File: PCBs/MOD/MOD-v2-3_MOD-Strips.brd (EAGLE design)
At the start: 50.8 x 25.4 mm, 11 parts

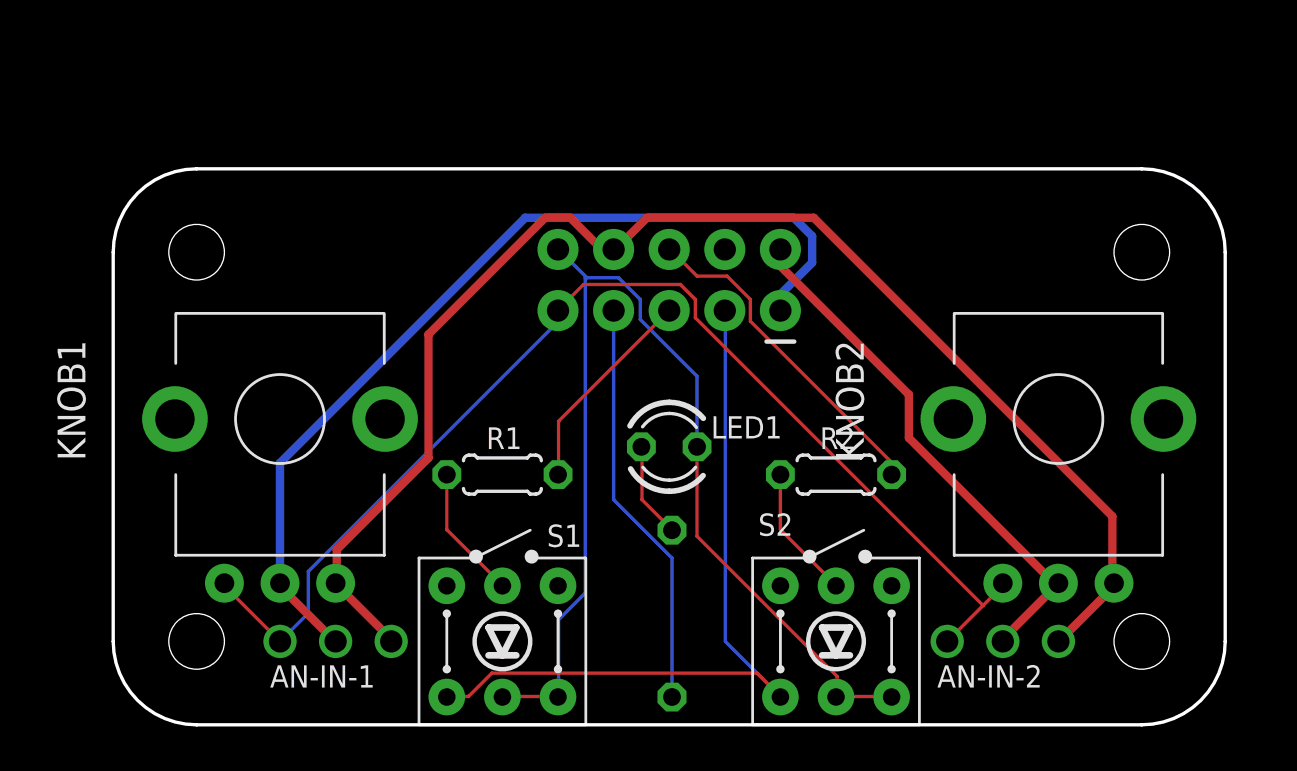
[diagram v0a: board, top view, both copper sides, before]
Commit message: new MOD teensy board
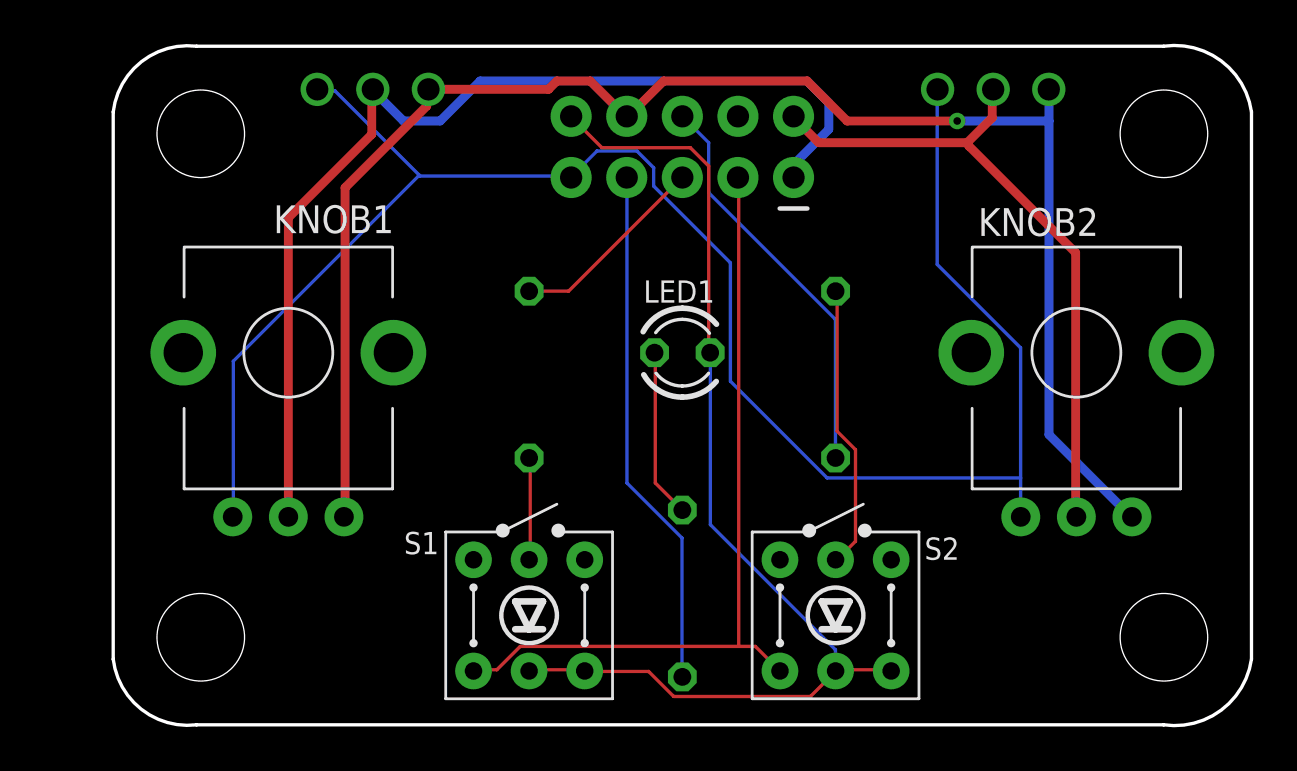
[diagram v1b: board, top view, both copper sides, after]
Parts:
- removed J1: (no value), SparkFun-Connectors:2X5-SHROUDED_LOCK
- added STRIP-MOD: (no value), SparkFun-Connectors:2X5-SHROUDED_LOCK
- R1, R2: device CMU-ArtFab:0204/5 -> CMU-ArtFab:0204/7
- moved AN-IN-1 25.3 mm to (9.32, 29.0), flipped to the bottom, turned to 180 degrees
- moved AN-IN-2 25.2 mm to (37.7, 29.0), flipped to the bottom, turned to 180 degrees
- moved R1 4.73 mm to (19.0, 16.0), flipped to the bottom, turned to 90 degrees
- moved R2 4.57 mm to (33.0, 16.0), flipped to the bottom, turned to 270 degrees
- moved LED1 4.34 mm to (26.0, 17.0)
- moved KNOB2 3.14 mm to (44.0, 17.0)
- moved KNOB1 3.05 mm to (8.00, 17.0)
- moved S1 1.70 mm to (19.0, 5.00)
- moved S2 1.19 mm to (33.0, 5.00)
- moved R4 1.03 mm to (26.0, 6.00)
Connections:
- net +3V3: now also STRIP-MOD.9; no longer J1.9
- net AGND: now also STRIP-MOD.8; no longer J1.8
- net AN1: now also STRIP-MOD.1; no longer J1.1
- net AN2: now also STRIP-MOD.2; no longer J1.2
- net B1: now also STRIP-MOD.3; no longer J1.3
- net B2: now also STRIP-MOD.4; no longer J1.4
- net GND: now also STRIP-MOD.10; no longer J1.10
- net LED1: now also STRIP-MOD.7; no longer J1.7
- net PWM_1: now also STRIP-MOD.5; no longer J1.5
- net PWM_2: now also STRIP-MOD.6; no longer J1.6
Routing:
- net +3V3: track 54.4 -> 84.4 mm
- net AGND: track 63.9 -> 72.8 mm, vias 0 -> 1
- net N$2: track 6.13 -> 13.1 mm
- net AN2: track 24.4 -> 30.5 mm
- net AN1: track 42.5 -> 47.8 mm
- net LED1: track 18.8 -> 23.9 mm
- net N1: track 4.38 -> 7.73 mm
- net PWM_2: track 15.4 -> 18.5 mm
- net B1: track 34.9 -> 36.4 mm
- net N$1: track 6.13 -> 4.71 mm
- net GND: track 51.4 -> 50.3 mm
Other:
- board size 50.8 x 25.4 mm -> 52 x 31.1 mm
